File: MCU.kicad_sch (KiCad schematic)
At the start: 2 parts, among them J1 FH34SRJ-8S-0.5SH_50_, U17 DEV-15583

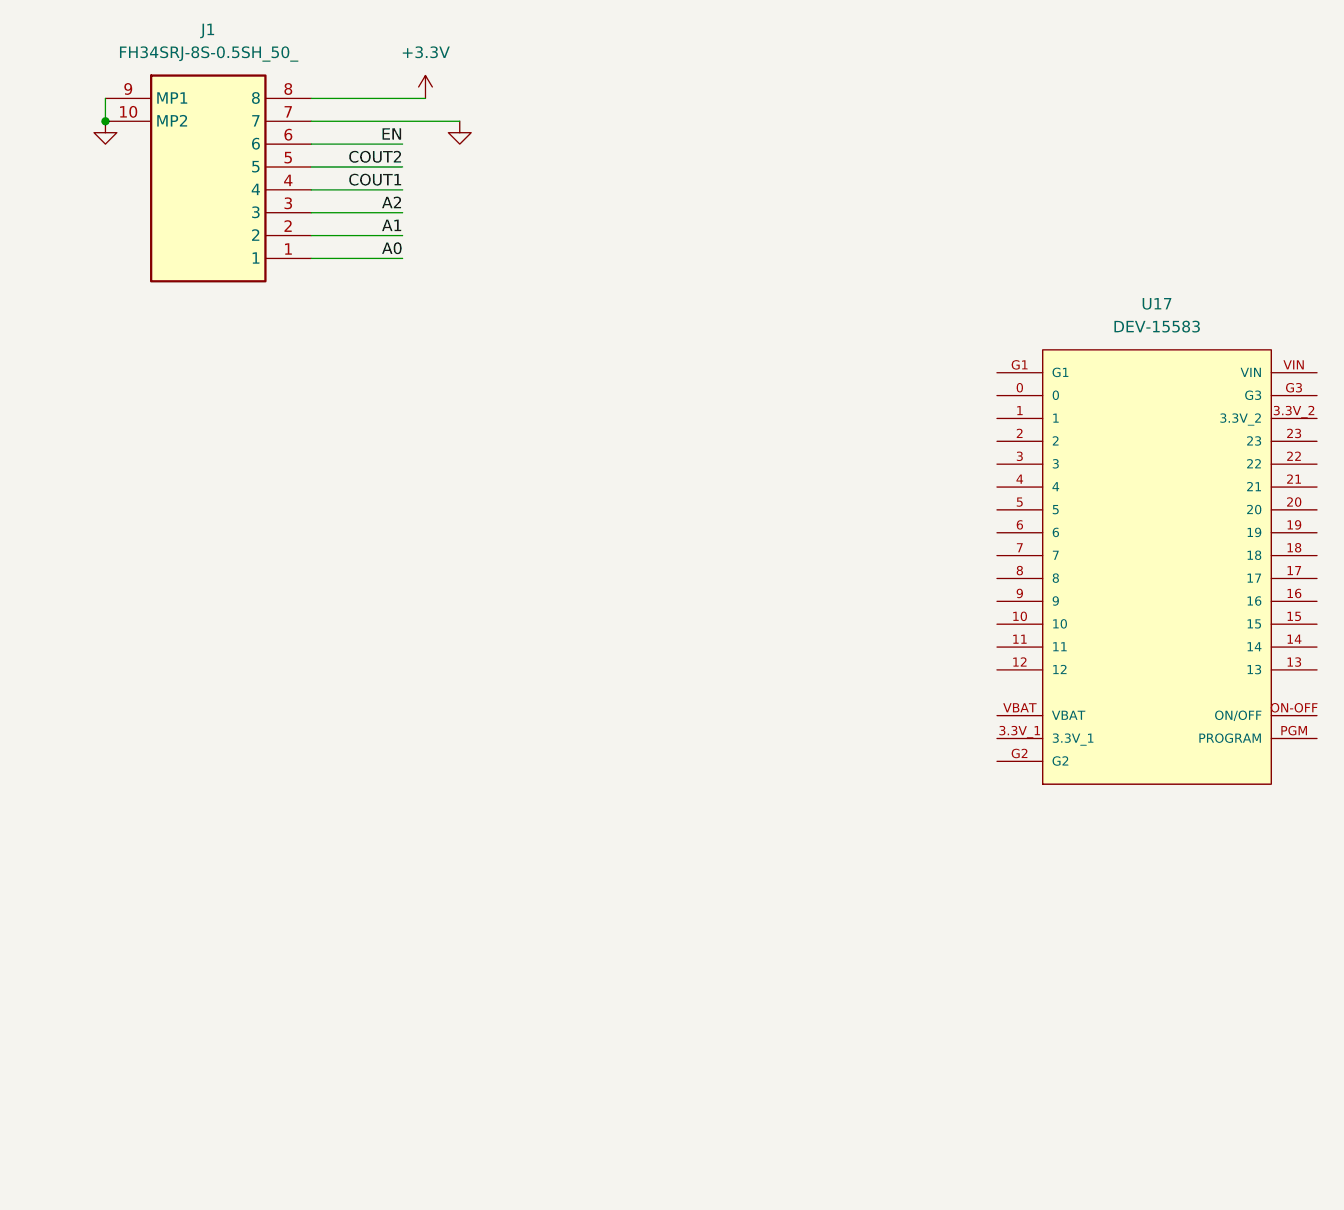
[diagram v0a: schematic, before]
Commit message: Started designing main schematic. Added DRV8833 circuit with 2 motors attached.
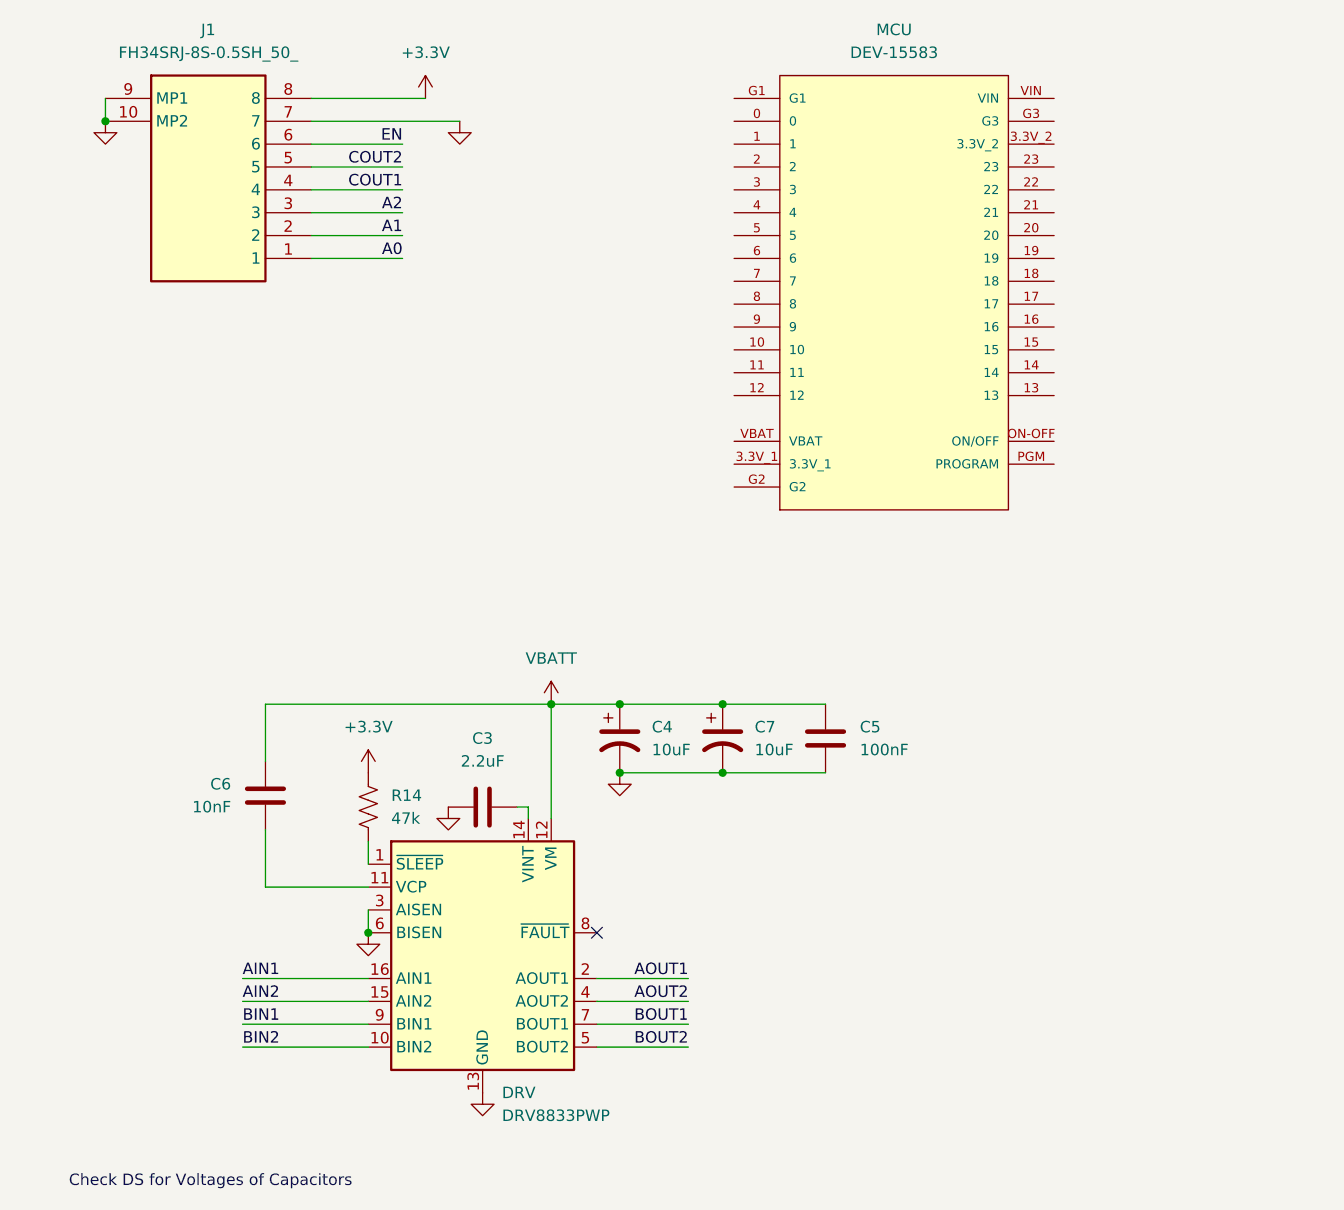
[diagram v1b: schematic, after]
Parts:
- added C3: 2.2uF, symbol Device:C
- added C4, C7: 10uF, symbol Device:C_Polarized_US
- added C5: 100nF, symbol Device:C
- added C6: 10nF, symbol Device:C
- added DRV: DRV8833PWP, Package_SO:HTSSOP-16-1EP_4.4x5mm_P0.65mm_EP3.4x5mm_Mask2.46x2.31mm_ThermalVias, symbol Driver_Motor:DRV8833PWP
- added R14: 47k, symbol Device:R_US
- renumbered U17 to MCU
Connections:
- net +3.3V: now also R14.1
- net GND: now also C3.1, C4.2, C5.1, C7.2, DRV.13 (GND), DRV.17 (GND), DRV.3 (AISEN), DRV.6 (BISEN)
- new net: C6.2, DRV.11 (VCP)
- new net: DRV.1 (~{SLEEP}), R14.2
- new net: C3.2, DRV.14 (VINT)
- new net AIN1: DRV.16 (AIN1)
- new net AIN2: DRV.15 (AIN2)
- new net AOUT1: DRV.2 (AOUT1)
- new net AOUT2: DRV.4 (AOUT2)
- new net BIN1: DRV.9 (BIN1)
- new net BIN2: DRV.10 (BIN2)
- new net BOUT1: DRV.7 (BOUT1)
- new net BOUT2: DRV.5 (BOUT2)
- new net VBATT: C4.1, C5.2, C6.1, C7.1, DRV.12 (VM)
- no-connect marks 0 -> 1
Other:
- note added: "Check DS for Voltages of Capacitors"
- moved on the sheet: MCU

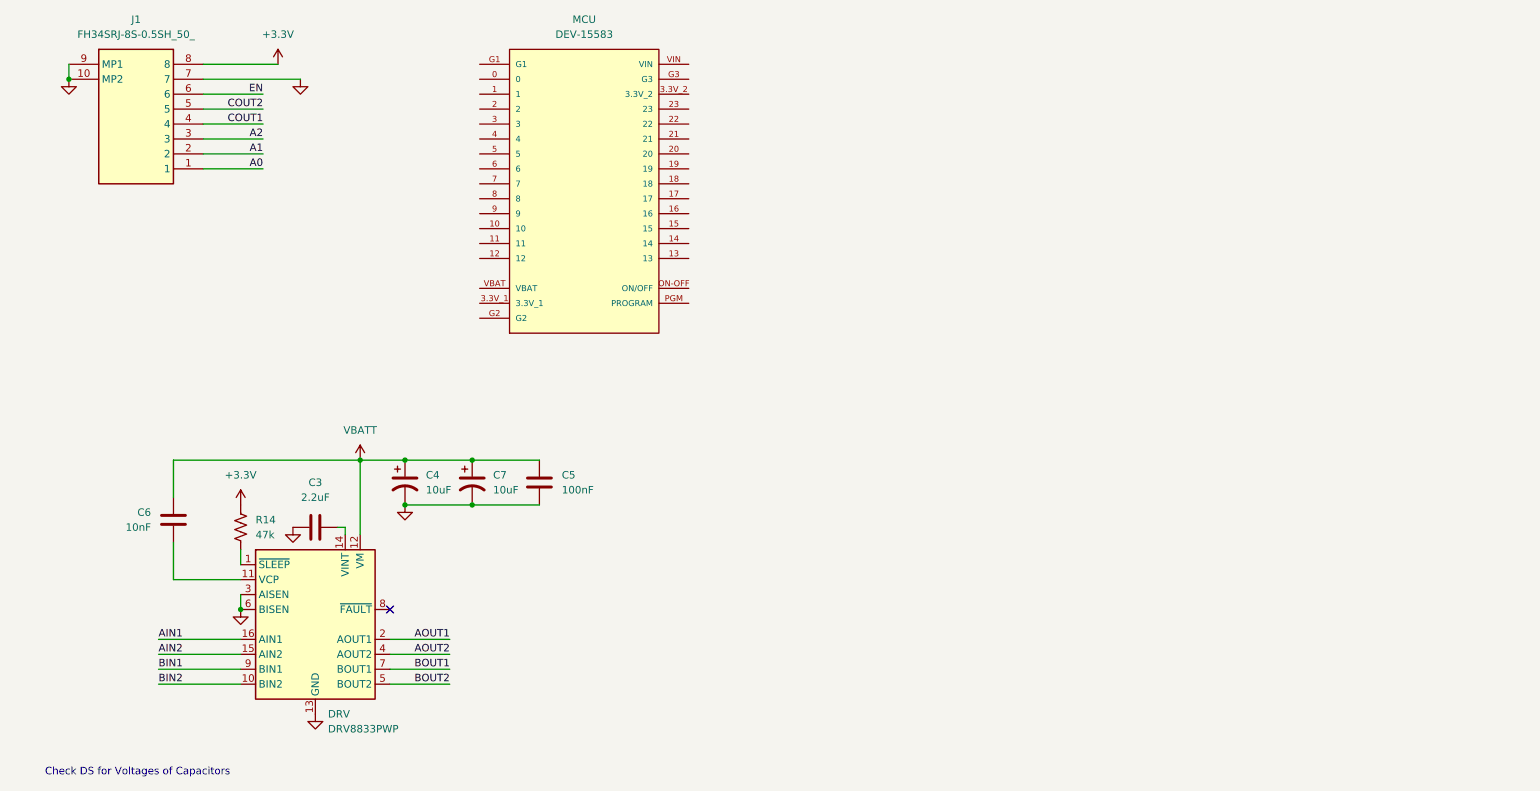
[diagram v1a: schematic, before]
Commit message: Added power regulation using buck DC-DC switching regulator MT2492 and an LDO LD1117S33CTR for clearing ripple.
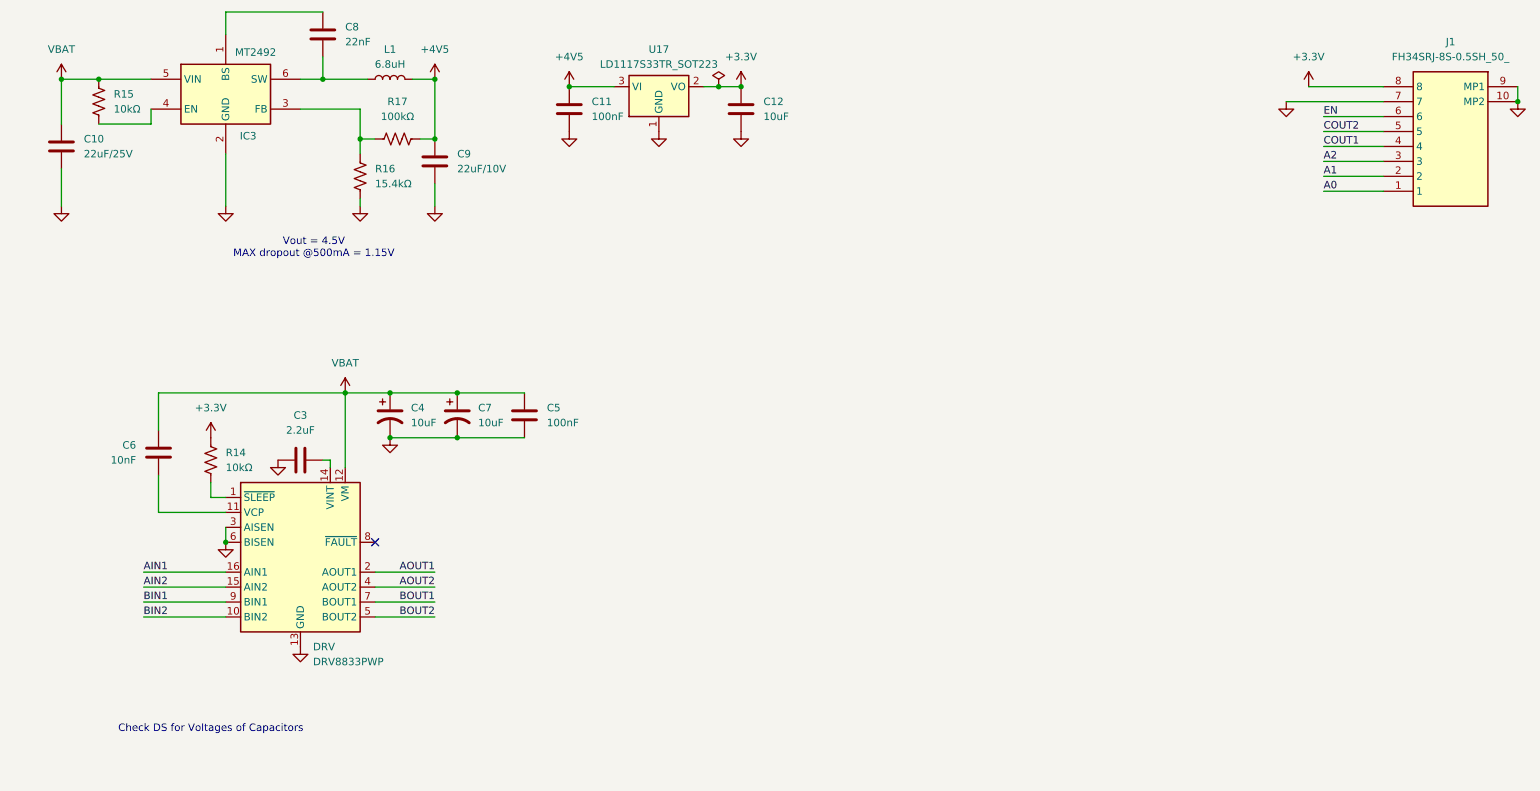
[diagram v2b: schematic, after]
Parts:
- removed MCU: DEV-15583, DEV-15583:MODULE_DEV-15583, symbol DEV-15583:DEV-15583
- added C10: 22uF/25V, symbol Device:C
- added C11: 100nF, symbol Device:C
- added C12: 10uF, symbol Device:C
- added C8: 22nF, symbol Device:C
- added C9: 22uF/10V, symbol Device:C
- added IC3: MT2492, SOT95P280X145-6N, symbol SAVITAR:MT2492
- added L1: 6.8uH, Inductor_SMD:L_1210_3225Metric_Pad1.42x2.65mm_HandSolder, symbol Device:L
- added R15: 10kΩ, symbol Device:R_US
- added R16: 15.4kΩ, symbol Device:R_US
- added R17: 100kΩ, symbol Device:R_US
- added U17: LD1117S33TR_SOT223, Package_TO_SOT_SMD:SOT-223-3_TabPin2, symbol Regulator_Linear:LD1117S33TR_SOT223
- R14: value 47k -> 10kΩ
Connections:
- net +3.3V: now also C12.2, U17.2 (VO)
- net GND: now also C10.2, C11.1, C12.1, C9.2, IC3.2 (GND), R16.2, U17.1 (GND)
- net VBATT renamed VBAT
- net VBAT: now also C10.1, IC3.5 (VIN), R15.1
- new net: C8.1, IC3.6 (SW), L1.1
- new net: C8.2, IC3.1 (BS)
- new net: IC3.4 (EN), R15.2
- new net: IC3.3 (FB), R16.1, R17.1
- new net +4V5: C11.2, C9.1, L1.2, R17.2, U17.3 (VI)
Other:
- note added: "Vout = 4.5V MAX dropout @500mA = 1.15V"
- moved on the sheet: C3, C4, C5, C6, C7, DRV, J1, R14
